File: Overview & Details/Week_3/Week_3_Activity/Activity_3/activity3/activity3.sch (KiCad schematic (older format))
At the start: 2 parts, among them J1 62684-502100ALF, U3 DISP_TFT_2.8IN_240x320_50PIN

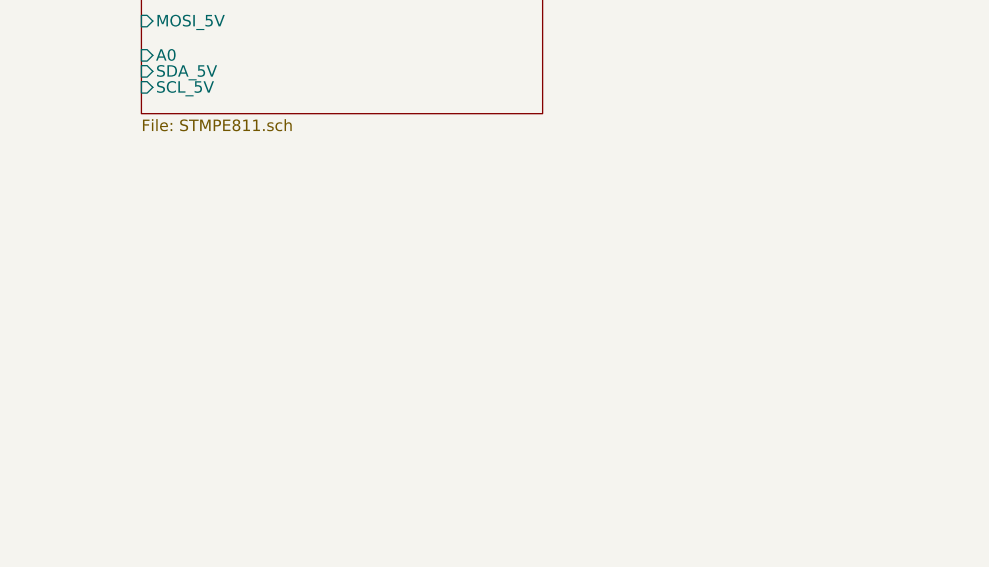
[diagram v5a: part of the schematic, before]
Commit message: added todo note on schematic
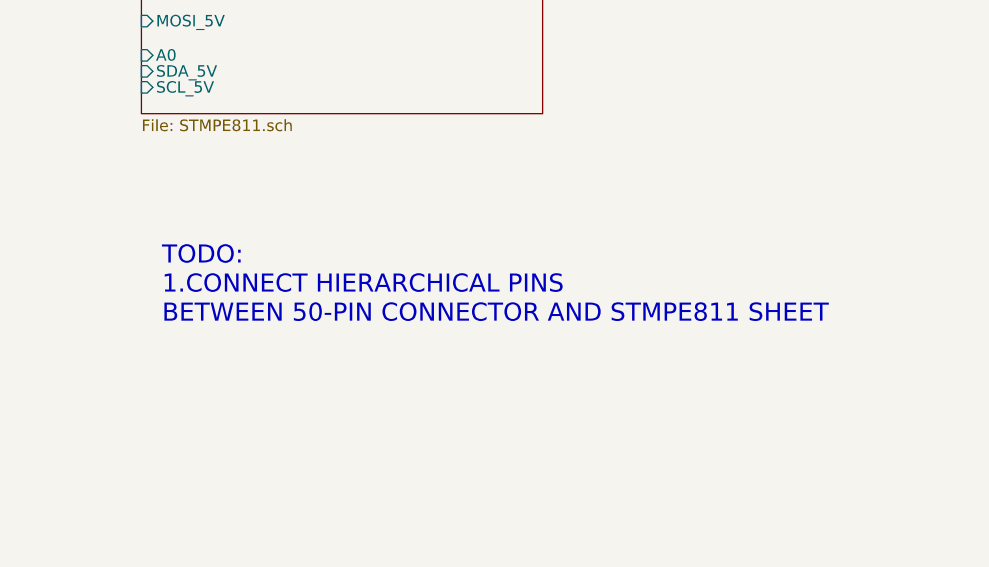
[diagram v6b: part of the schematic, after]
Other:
- note added: "TODO:\n1.CONNECT HIERARCHICAL PINS\nBETWEEN 50-PIN CONNECTOR AND STMPE811 SHEET"
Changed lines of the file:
@@
 Text HLabel 6000 6020 2    79   Input ~ 0
 Y-
+Text Notes 7420 3310 0    79   ~ 0
+TODO:\n1.CONNECT HIERARCHICAL PINS\nBETWEEN 50-PIN CONNECTOR AND STMPE811 SHEET
 $EndSCHEMATC

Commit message: linked symbol to footprint for 50pin connector and controller
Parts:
- J1: footprint CONN50_62684-502100ALF -> Display_Board:62684-502100ALF
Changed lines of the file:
@@
 F 0 "J1" H 6300 1570 60  0000 L CNN
 F 1 "62684-502100ALF" H 6050 1630 60  0000 L CNN
-F 2 "CONN50_62684-502100ALF" H 6400 -1040 60  0001 C CNN
+F 2 "Display_Board:62684-502100ALF" H 6400 -1040 60  0001 C CNN
 F 3 "" H 6000 1420 60  0000 C CNN
 	1    6000 1420
